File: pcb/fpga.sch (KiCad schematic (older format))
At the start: 61 parts, among them J2 Micro_SD_Card, P1 JTAG_CONN, U12 10CL025YE144C8N, U13 IS25LP016D-JBLE, U15 TLV70012, U16 TLV70025, U17 TLV70012

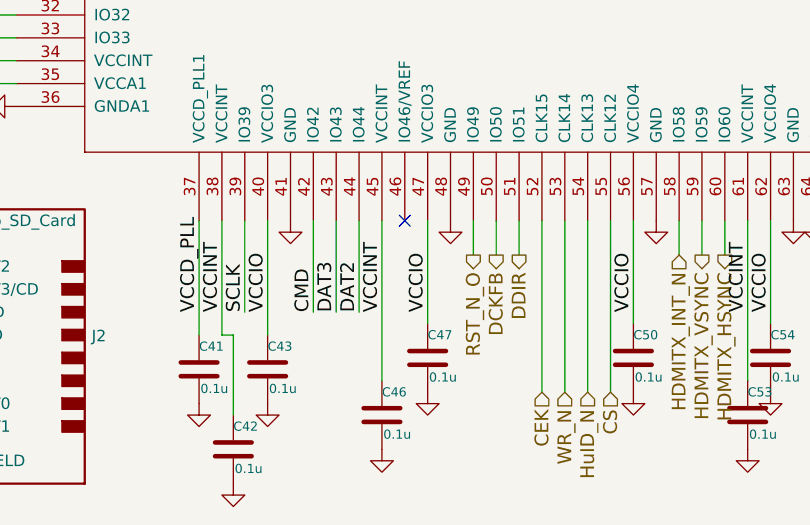
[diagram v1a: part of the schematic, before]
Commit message: Added CDD signal to last open IO pin
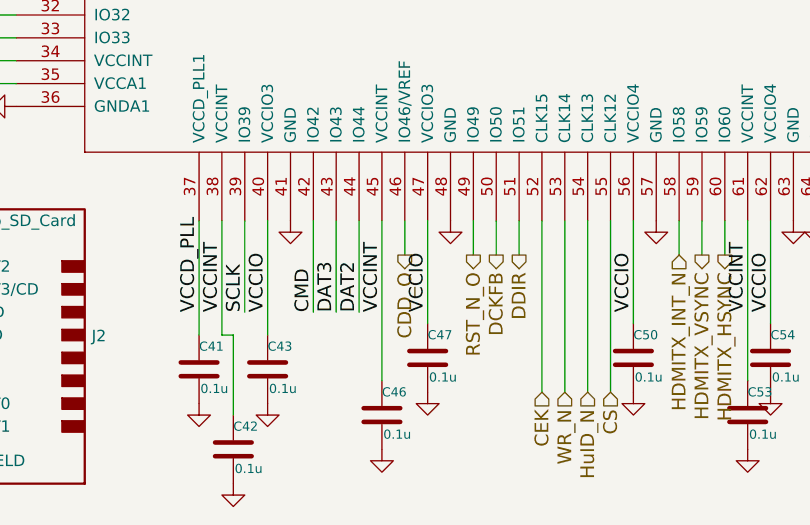
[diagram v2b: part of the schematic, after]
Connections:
- net labels added: CDD_O
- wire segments 222 -> 223
- no-connect marks 4 -> 3
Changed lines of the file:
@@
 Sheet 2 5
 Title "PCEHD"
-Date "2020-01-03"
+Date "2020-01-18"
 Rev "0.1"
 Comp ""
@@
 Wire Wire Line
 	5300 6500 5300 6350
-NoConn ~ 3400 6350
 Wire Wire Line
 	5900 6350 5900 6500
+Wire Wire Line
+	3400 6350 3400 6500
+Text HLabel 3400 6500 3    60   Output ~ 0
+CDD_O
 Wire Bus Line
 	10650 1900 10650 2500
